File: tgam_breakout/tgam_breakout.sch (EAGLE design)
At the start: 14 parts, among them X1 332-06, X2 332-10

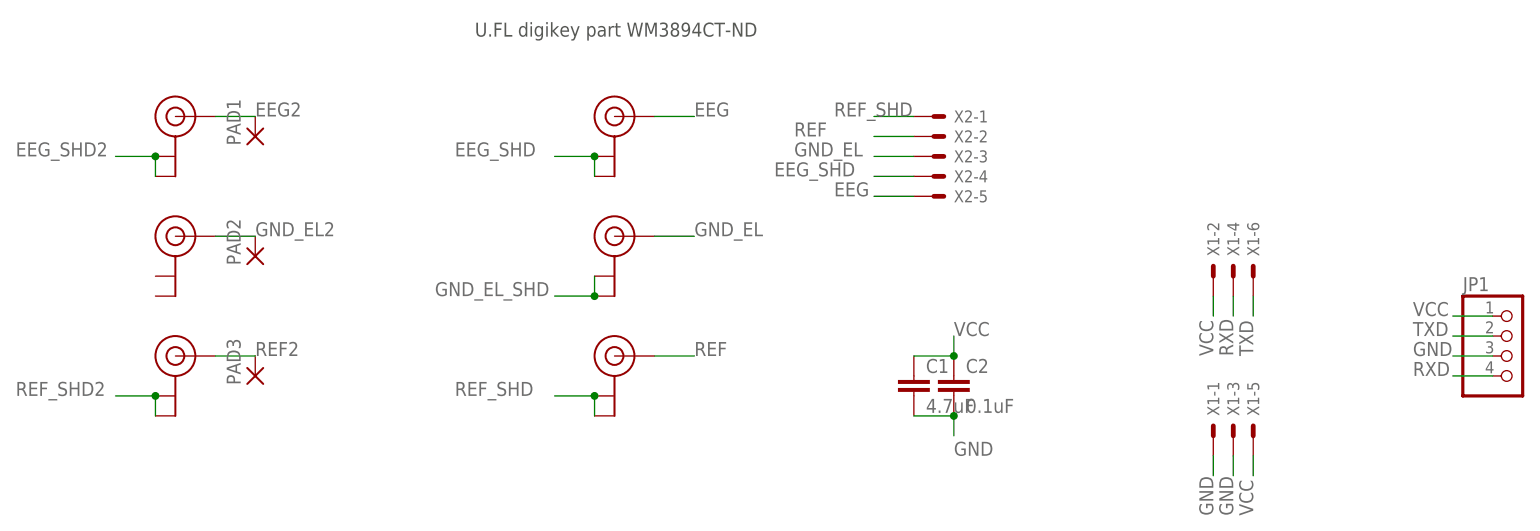
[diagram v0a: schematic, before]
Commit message: seems some inconsistencies were left over
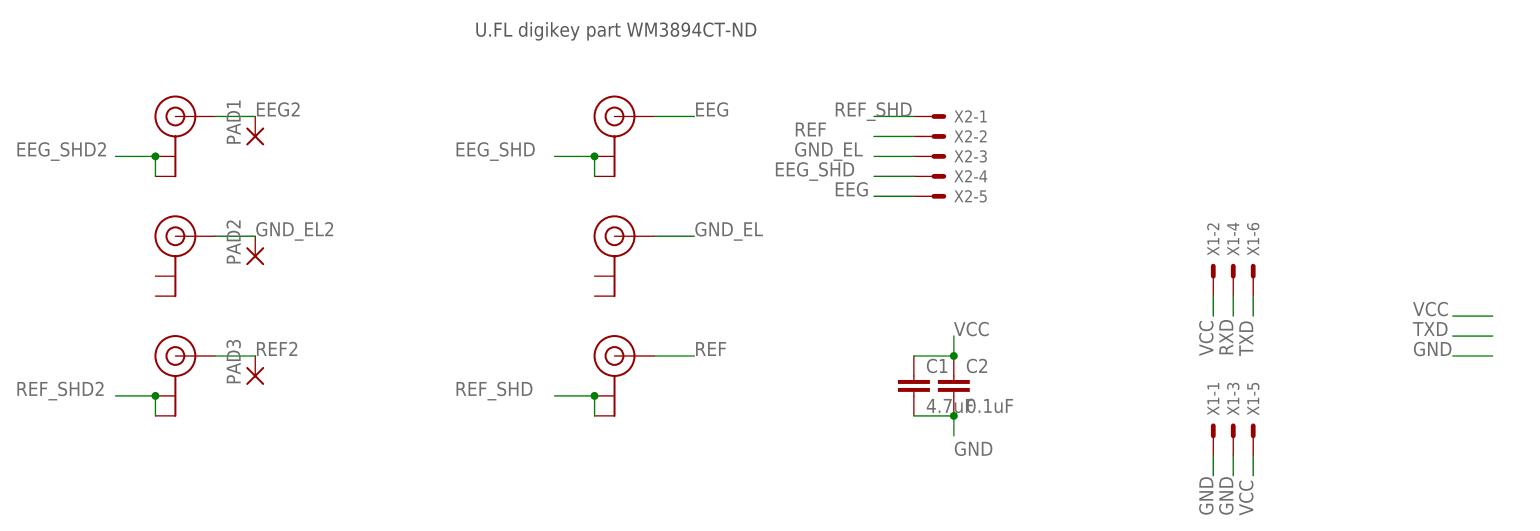
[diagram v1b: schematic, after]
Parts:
- removed JP1: (no value), pinhead:PINHD-1X4
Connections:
- removed net GND_EL_SHD: GND_EL.GND@0, GND_EL.GND@1
- net GND: no longer JP1.3
- net RXD: no longer JP1.4
- net TXD: no longer JP1.2
- net VCC: no longer JP1.1
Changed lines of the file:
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@@
 <part name="GND_ELEL" library="SparkFun-Connectors" deviceset="U.FL" device=""/>
 <part name="REF_EL" library="SparkFun-Connectors" deviceset="U.FL" device=""/>
-<part name="JP1" library="pinhead" deviceset="PINHD-1X4" device=""/>
 <part name="PAD1" library="wirepad" deviceset="SMD5" device=""/>
 <part name="PAD2" library="wirepad" deviceset="SMD5" device=""/>
@@
 <instance part="GND_ELEL" gate="G$1" x="-27.94" y="48.26"/>
 <instance part="REF_EL" gate="G$1" x="-27.94" y="33.02"/>
-<instance part="JP1" gate="A" x="142.24" y="33.02"/>
 <instance part="PAD1" gate="1" x="-17.78" y="60.96" rot="R90"/>
 <instance part="PAD2" gate="1" x="-17.78" y="45.72" rot="R90"/>
@@
 </segment>
 <segment>
-<pinref part="JP1" gate="A" pin="1"/>
 <wire x1="139.7" y1="38.1" x2="134.62" y2="38.1" width="0.1524" layer="91"/>
 <label x="129.54" y="38.1" size="1.778" layer="95"/>
@@
 <label x="106.68" y="33.02" size="1.778" layer="95" rot="R90"/>
 </segment>
-<segment>
-<pinref part="JP1" gate="A" pin="4"/>
-<wire x1="139.7" y1="30.48" x2="134.62" y2="30.48" width="0.1524" layer="91"/>
-<label x="129.54" y="30.48" size="1.778" layer="95"/>
-</segment>
 </net>
 <net name="TXD" class="0">
@@
 </segment>
 <segment>
-<pinref part="JP1" gate="A" pin="2"/>
 <wire x1="139.7" y1="35.56" x2="134.62" y2="35.56" width="0.1524" layer="91"/>
 <label x="129.54" y="35.56" size="1.778" layer="95"/>
@@
 </segment>
 <segment>
-<pinref part="JP1" gate="A" pin="3"/>
 <wire x1="139.7" y1="33.02" x2="134.62" y2="33.02" width="0.1524" layer="91"/>
 <label x="129.54" y="33.02" size="1.778" layer="95"/>
@@
 </segment>
 </net>
-<net name="GND_EL_SHD" class="0">
-<segment>
-<pinref part="GND_EL" gate="G$1" pin="GND@0"/>
-<pinref part="GND_EL" gate="G$1" pin="GND@1"/>
-<wire x1="25.4" y1="43.18" x2="25.4" y2="40.64" width="0.1524" layer="91"/>
-<wire x1="25.4" y1="40.64" x2="20.32" y2="40.64" width="0.1524" layer="91"/>
-<junction x="25.4" y="40.64"/>
-<label x="5.08" y="40.64" size="1.778" layer="95"/>
-</segment>
-</net>

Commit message: Oh fsck! I had switched reference electrode and shield connections...
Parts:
- added JP1: (no value), pinhead:PINHD-1X4
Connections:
- net GND: now also GND_EL.GND@0, GND_EL.GND@1, JP1.3
- net REF: now also X2-1.S; no longer X2-2.S
- net REF_SHD: now also X2-2.S; no longer X2-1.S
- net RXD: now also JP1.4
- net TXD: now also JP1.2
- net VCC: now also JP1.1
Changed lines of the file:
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@@
 <part name="PAD2" library="wirepad" deviceset="SMD5" device=""/>
 <part name="PAD3" library="wirepad" deviceset="SMD5" device=""/>
+<part name="JP1" library="pinhead" deviceset="PINHD-1X4" device=""/>
 </parts>
 <sheets>
@@
 <instance part="PAD2" gate="1" x="-17.78" y="45.72" rot="R90"/>
 <instance part="PAD3" gate="1" x="-17.78" y="30.48" rot="R90"/>
+<instance part="JP1" gate="A" x="142.24" y="33.02"/>
 </instances>
 <busses>
@@
 </segment>
 <segment>
-<pinref part="X2" gate="-1" pin="S"/>
-<wire x1="66.04" y1="63.5" x2="60.96" y2="63.5" width="0.1524" layer="91"/>
-<label x="55.88" y="63.5" size="1.778" layer="95"/>
+<pinref part="X2" gate="-2" pin="S"/>
+<wire x1="66.04" y1="60.96" x2="60.96" y2="60.96" width="0.1524" layer="91"/>
+<label x="48.26" y="60.96" size="1.778" layer="95"/>
 </segment>
 </net>
@@
 </segment>
 <segment>
-<pinref part="X2" gate="-2" pin="S"/>
-<wire x1="66.04" y1="60.96" x2="60.96" y2="60.96" width="0.1524" layer="91"/>
-<label x="50.8" y="60.96" size="1.778" layer="95"/>
+<pinref part="X2" gate="-1" pin="S"/>
+<wire x1="66.04" y1="63.5" x2="60.96" y2="63.5" width="0.1524" layer="91"/>
+<label x="55.88" y="63.5" size="1.778" layer="95"/>
 </segment>
 </net>
@@
 <wire x1="139.7" y1="38.1" x2="134.62" y2="38.1" width="0.1524" layer="91"/>
 <label x="129.54" y="38.1" size="1.778" layer="95"/>
+<pinref part="JP1" gate="A" pin="1"/>
 </segment>
 </net>
@@
 <wire x1="106.68" y1="40.64" x2="106.68" y2="38.1" width="0.1524" layer="91"/>
 <label x="106.68" y="33.02" size="1.778" layer="95" rot="R90"/>
+</segment>
+<segment>
+<pinref part="JP1" gate="A" pin="4"/>
+<wire x1="139.7" y1="30.48" x2="134.62" y2="30.48" width="0.1524" layer="91"/>
+<label x="129.54" y="30.48" size="1.778" layer="95"/>
 </segment>
 </net>
@@
 <wire x1="139.7" y1="35.56" x2="134.62" y2="35.56" width="0.1524" layer="91"/>
 <label x="129.54" y="35.56" size="1.778" layer="95"/>
+<pinref part="JP1" gate="A" pin="2"/>
 </segment>
 </net>
@@
 <wire x1="139.7" y1="33.02" x2="134.62" y2="33.02" width="0.1524" layer="91"/>
 <label x="129.54" y="33.02" size="1.778" layer="95"/>
+<pinref part="JP1" gate="A" pin="3"/>
+</segment>
+<segment>
+<pinref part="GND_EL" gate="G$1" pin="GND@1"/>
+<pinref part="GND_EL" gate="G$1" pin="GND@0"/>
+<wire x1="25.4" y1="40.64" x2="25.4" y2="43.18" width="0.1524" layer="91"/>
+<wire x1="25.4" y1="43.18" x2="20.32" y2="43.18" width="0.1524" layer="91"/>
+<junction x="25.4" y="43.18"/>
+<label x="15.24" y="43.18" size="1.778" layer="95"/>
 </segment>
 </net>
